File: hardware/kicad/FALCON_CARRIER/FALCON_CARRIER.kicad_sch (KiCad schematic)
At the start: 39 parts, among them J1 POWER_INPUT, J10 LEAK_SENSOR_TBD, J11 FAN_TBD, J12 SERVICE_I2C, J2 BAR02_I2C, J3 GPS_UART, J4 INA260_BAT_LOGIC, J5 INA260_SOLAR_0X41, J6 MCP9808_0X18, J7 ANEMOMETER, J8 WIND_VANE, J9 DS18B20_OPTION, U1 REGULATOR_3V3_TBD, U2 ESP32_DEVKITC_V4_WROOM32E, U3 BNO085_SPI, U4 ADS1115_0X48, U5 FAN_DRIVER_TBD, U6 EFUSE_TPS25947_TBD

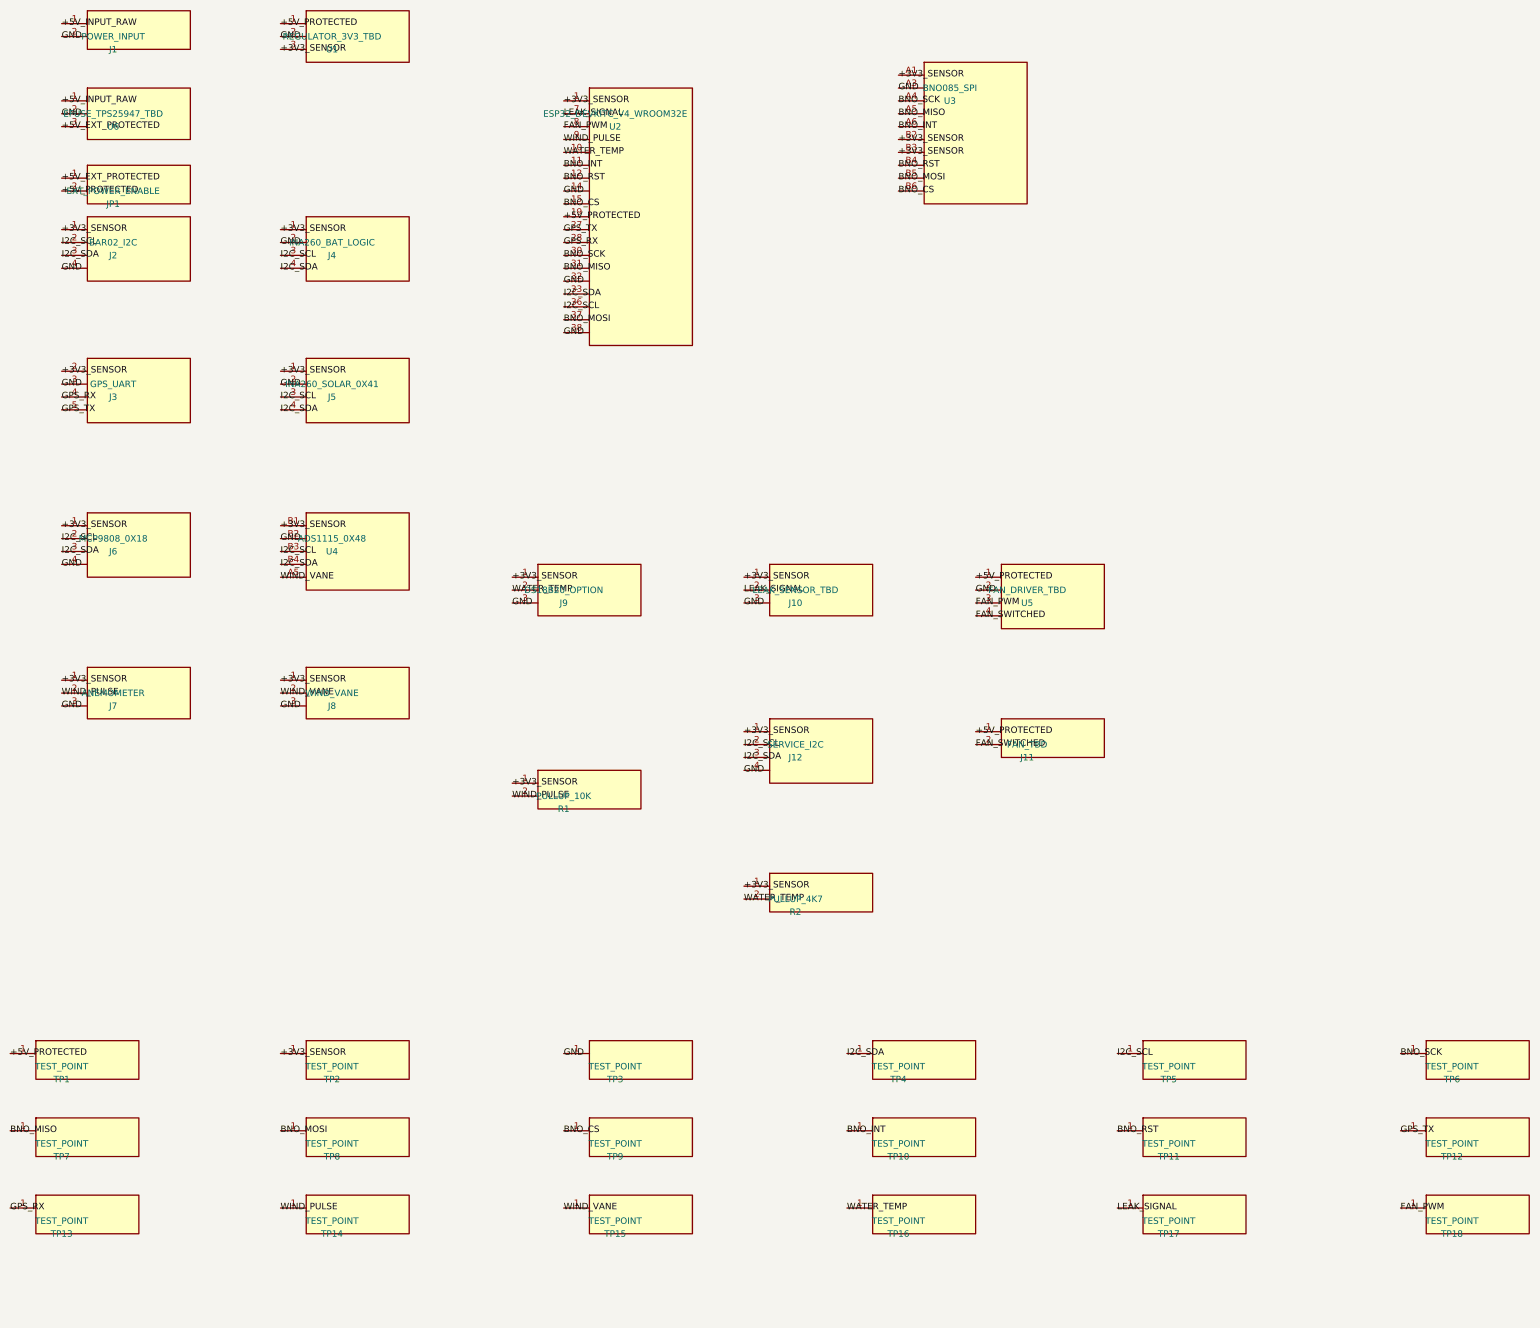
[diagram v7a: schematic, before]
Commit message: Implement dual four-wire fan interface
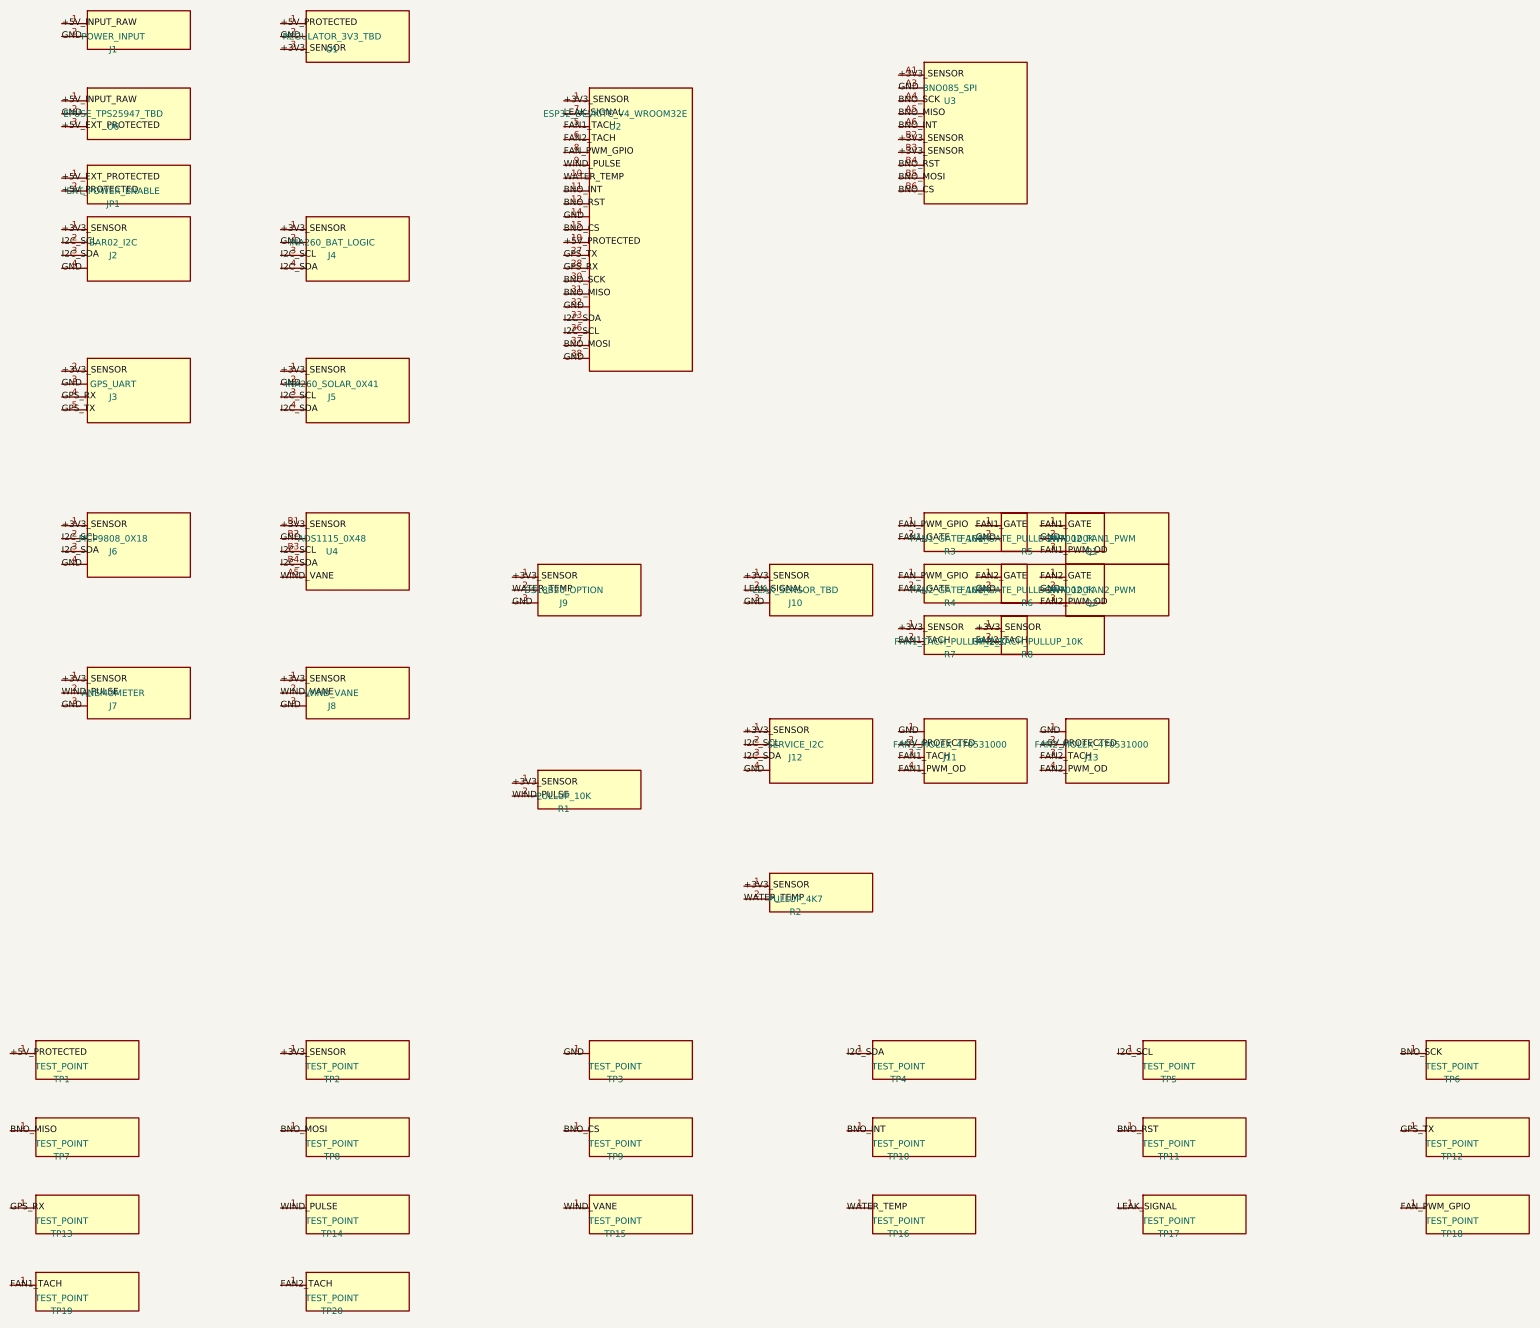
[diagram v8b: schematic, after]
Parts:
- removed U5: FAN_DRIVER_TBD, symbol FALCON:FAN_DRIVER_TBD
- added J13: FAN2_MOLEX_470531000, symbol FALCON:FAN2_MOLEX_470531000
- added Q1: 2N7002_FAN1_PWM, symbol FALCON:2N7002_FAN1_PWM
- added Q2: 2N7002_FAN2_PWM, symbol FALCON:2N7002_FAN2_PWM
- added R3: FAN1_GATE_100R, symbol FALCON:FAN1_GATE_100R
- added R4: FAN2_GATE_100R, symbol FALCON:FAN2_GATE_100R
- added R5: FAN1_GATE_PULLDOWN_100K, symbol FALCON:FAN1_GATE_PULLDOWN_100K
- added R6: FAN2_GATE_PULLDOWN_100K, symbol FALCON:FAN2_GATE_PULLDOWN_100K
- added R7: FAN1_TACH_PULLUP_10K, symbol FALCON:FAN1_TACH_PULLUP_10K
- added R8: FAN2_TACH_PULLUP_10K, symbol FALCON:FAN2_TACH_PULLUP_10K
- added TP19, TP20: TEST_POINT, symbol FALCON:TEST_POINT
- J11: value FAN_TBD -> FAN1_MOLEX_470531000; symbol FALCON:FAN_TBD -> FALCON:FAN1_MOLEX_470531000
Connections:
- net FAN_SWITCHED is gone; now on net +5V_PROTECTED: J11.2 (+5V_PROTECTED)
- net +3V3_SENSOR: now also R7.1 (+3V3_SENSOR), R8.1 (+3V3_SENSOR)
- net +5V_PROTECTED: now also J13.2 (+5V_PROTECTED); no longer J11.1 (+5V_PROTECTED)
- net GND: now also J11.1 (GND), J13.1 (GND), Q1.2 (GND), Q2.2 (GND), R5.2 (GND), R6.2 (GND)
- net FAN_PWM renamed FAN_PWM_GPIO
- net FAN_PWM_GPIO: now also R3.1 (FAN_PWM_GPIO), R4.1 (FAN_PWM_GPIO)
- new net FAN1_GATE: Q1.1 (FAN1_GATE), R3.2 (FAN1_GATE), R5.1 (FAN1_GATE)
- new net FAN1_PWM_OD: J11.4 (FAN1_PWM_OD), Q1.3 (FAN1_PWM_OD)
- new net FAN1_TACH: J11.3 (FAN1_TACH), R7.2 (FAN1_TACH), TP19.1 (+5V_PROTECTED), U2.5 (FAN1_TACH)
- new net FAN2_GATE: Q2.1 (FAN2_GATE), R4.2 (FAN2_GATE), R6.1 (FAN2_GATE)
- new net FAN2_PWM_OD: J13.4 (FAN2_PWM_OD), Q2.3 (FAN2_PWM_OD)
- new net FAN2_TACH: J13.3 (FAN2_TACH), R8.2 (FAN2_TACH), TP20.1 (+5V_PROTECTED), U2.6 (FAN2_TACH)
